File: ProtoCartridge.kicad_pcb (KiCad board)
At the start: 2 copper layers, 64.8 x 55.9 mm, 339 parts, among them J1 Cartridge Connector, U1 W25Q128

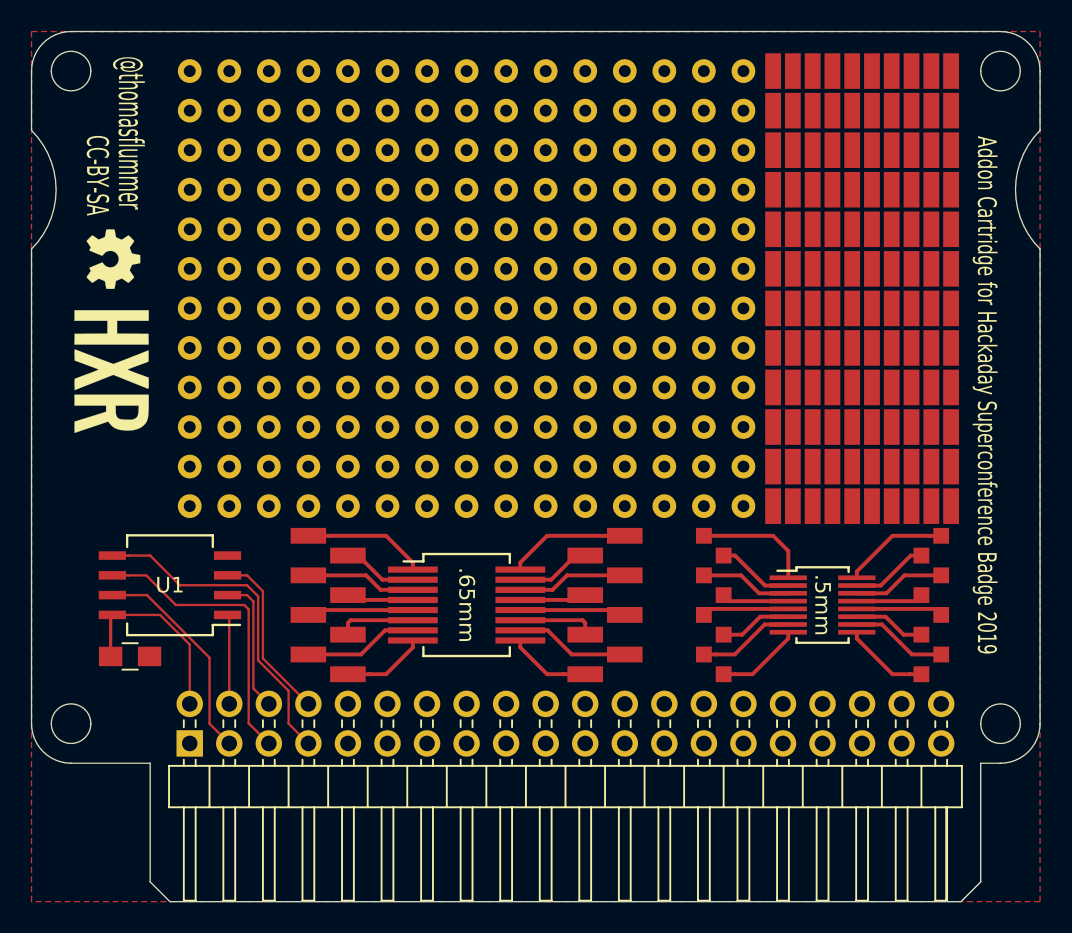
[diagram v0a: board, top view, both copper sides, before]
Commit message: Fixed error in cartridge connector pin assignments
Updated to version 1.2
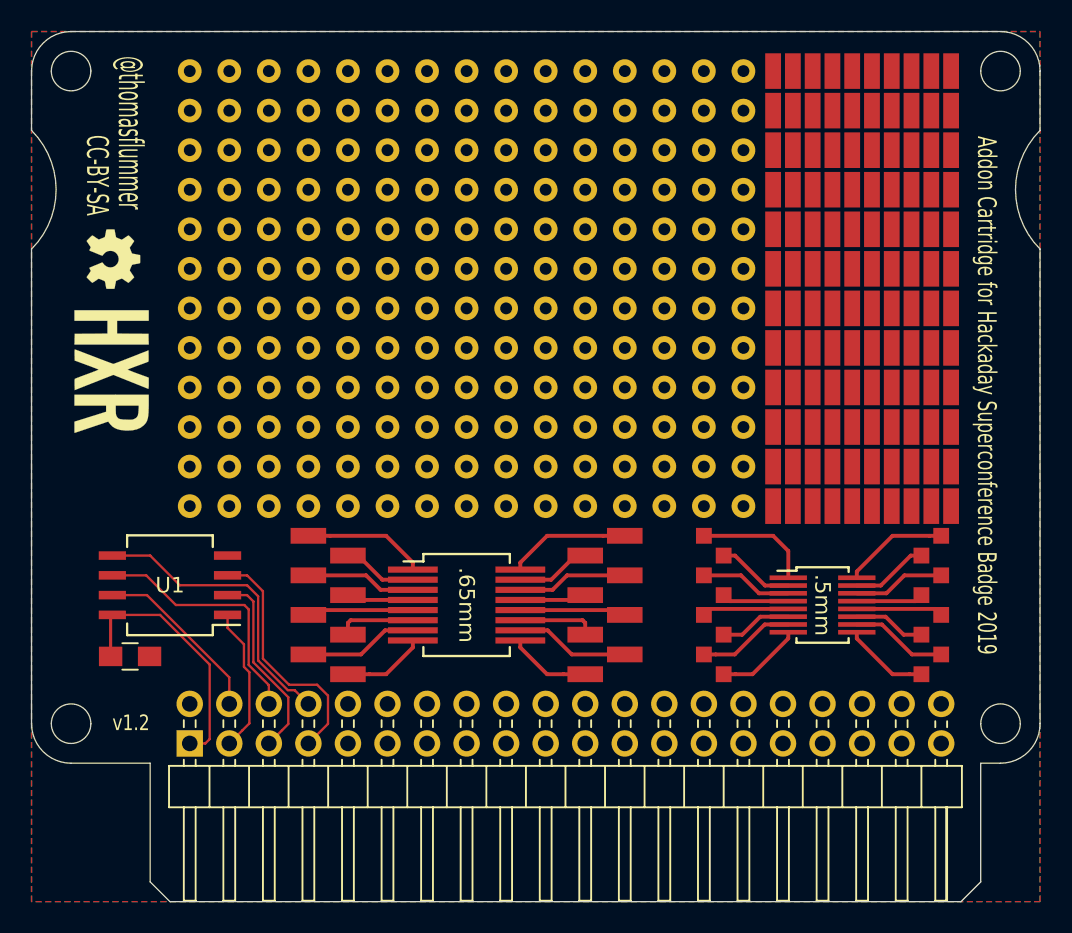
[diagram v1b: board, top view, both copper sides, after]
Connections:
- J1 pad 1: GND -> +3V3
- J1 pad 2: +3V3 -> GND
- J1 pad 3: F_HOLD -> F_CS
- J1 pad 39: +5V -> +BATT
- J1 pad 4: F_CS -> F_HOLD
- J1 pad 40: +BATT -> +5V
- J1 pad 5: F_SCK -> F_MISO
- J1 pad 6: F_MISO -> F_SCK
- J1 pad 7: F_MOSI -> F_WP
- J1 pad 8: F_WP -> F_MOSI
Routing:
- net F_WP: track 11.1 -> 15.8 mm
- net +3V3: track 12.3 -> 16.5 mm
- net F_CS: track 5.76 -> 9.52 mm
- net F_MISO: track 8.82 -> 12.4 mm
- net F_SCK: track 18.8 -> 16.3 mm
- net F_HOLD: track 13.9 -> 11.4 mm
- net F_MOSI: track 21.2 -> 18.9 mm
- added copper zone on B.Cu, net GND
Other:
- board text added: "v1.2"
